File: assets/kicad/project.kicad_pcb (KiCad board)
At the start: 2 copper layers, 150.2 x 91.2 mm, 27 parts, among them J1 Adafruit microSD, J2 EPD, J3 RTC

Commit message: added delay
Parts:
- renumbered R2 to R1, R1 to R2
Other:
- board text added: "21.06.2025"
- board text added: "Alessandro Crugnola"
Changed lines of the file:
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@@
 		(property "Value" "RTC"
 			(at 17.526 6.35 0)
-			(layer "F.Fab")
+			(layer "F.SilkS")
 			(effects
 				(font
@@
 		(descr "Resistor, Axial_DIN0207 series, Axial, Horizontal, pin pitch=7.62mm, 0.25W = 1/4W, length*diameter=6.3*2.5mm^2, http://cdn-reichelt.de/documents/datenblatt/B400/1_4W%23YAG.pdf")
 		(tags "Resistor Axial_DIN0207 series Axial Horizontal pin pitch 7.62mm 0.25W = 1/4W length 6.3mm diameter 2.5mm")
-		(property "Reference" "R2"
+		(property "Reference" "R1"
 			(at 3.81 -2.37 0)
 			(layer "F.SilkS")
@@
 		(descr "Resistor, Axial_DIN0207 series, Axial, Horizontal, pin pitch=7.62mm, 0.25W = 1/4W, length*diameter=6.3*2.5mm^2, http://cdn-reichelt.de/documents/datenblatt/B400/1_4W%23YAG.pdf")
 		(tags "Resistor Axial_DIN0207 series Axial Horizontal pin pitch 7.62mm 0.25W = 1/4W length 6.3mm diameter 2.5mm")
-		(property "Reference" "R1"
+		(property "Reference" "R2"
 			(at 3.81 -2.37 0)
 			(layer "F.SilkS")
@@
 		)
 	)
+	(gr_text "21.06.2025"
+		(at 206.756 193.548 0)
+		(layer "Cmts.User")
+		(effects
+			(font
+				(size 1 1)
+				(thickness 0.1)
+			)
+			(justify left bottom)
+		)
+	)
+	(gr_text "Alessandro Crugnola"
+		(at 178.054 172.212 0)
+		(layer "Cmts.User")
+		(effects
+			(font
+				(size 2 2)
+				(thickness 0.1)
+			)
+			(justify left bottom)
+		)
+	)
+	(gr_text "Photo Frame"
+		(at 186.69 190.5 0)
+		(layer "Cmts.User")
+		(effects
+			(font
+				(size 2 2)
+				(thickness 0.25)
+			)
+			(justify left bottom)
+		)
+	)

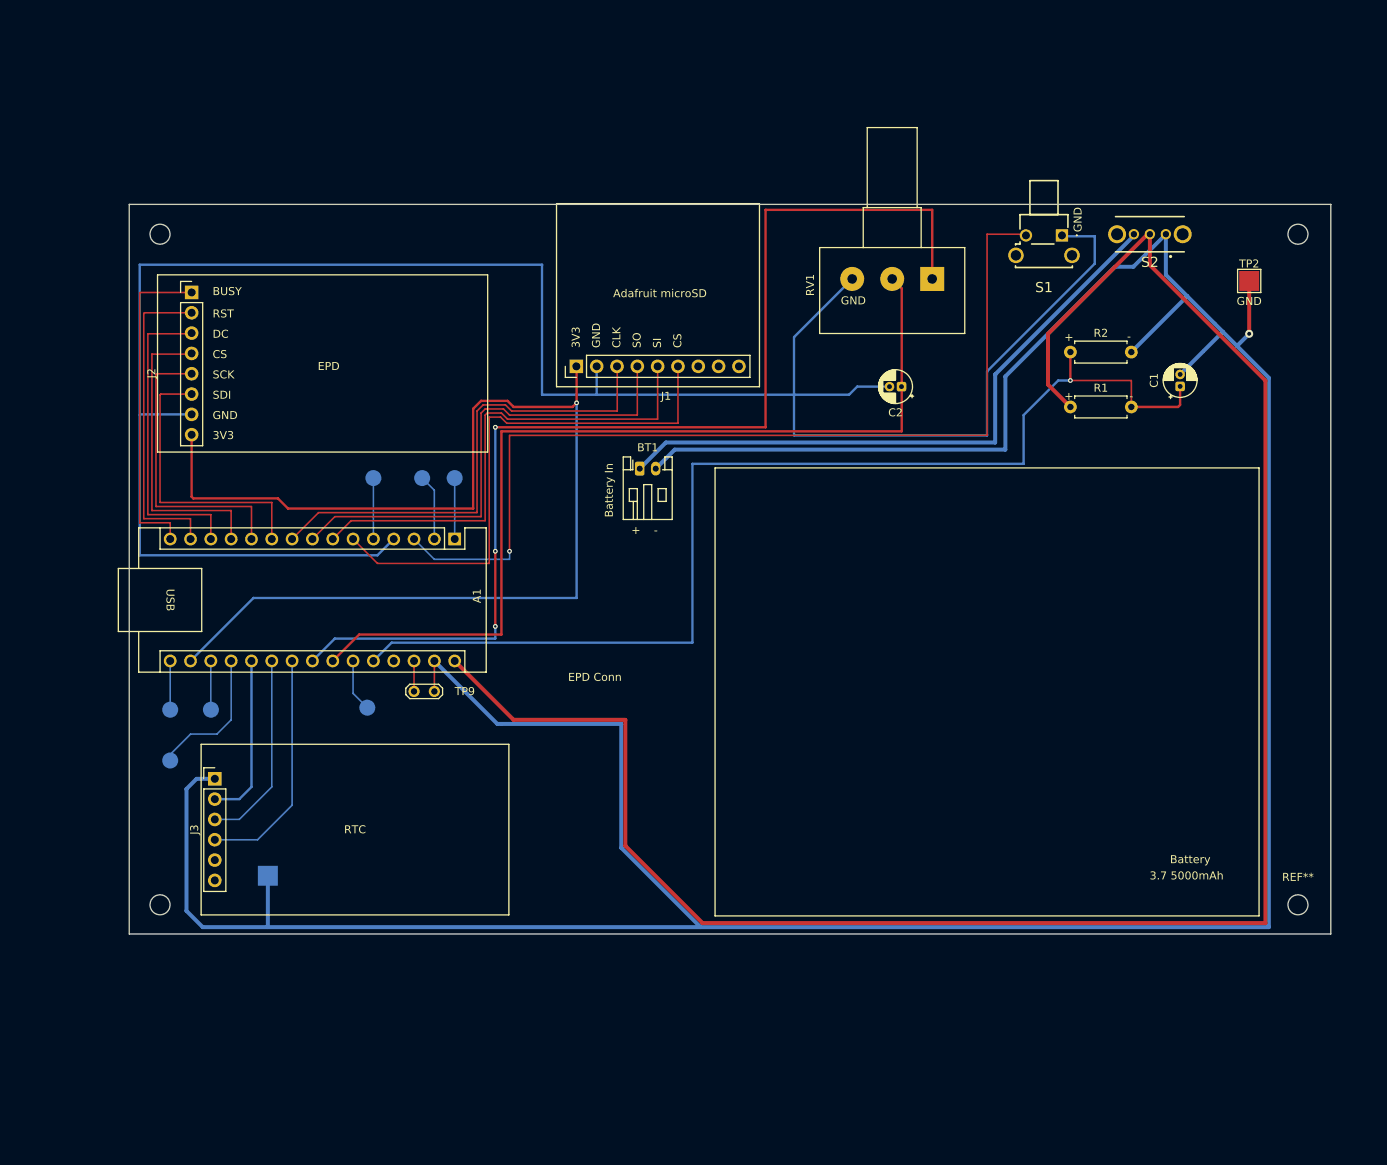
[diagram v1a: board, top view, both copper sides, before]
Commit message: updated pins
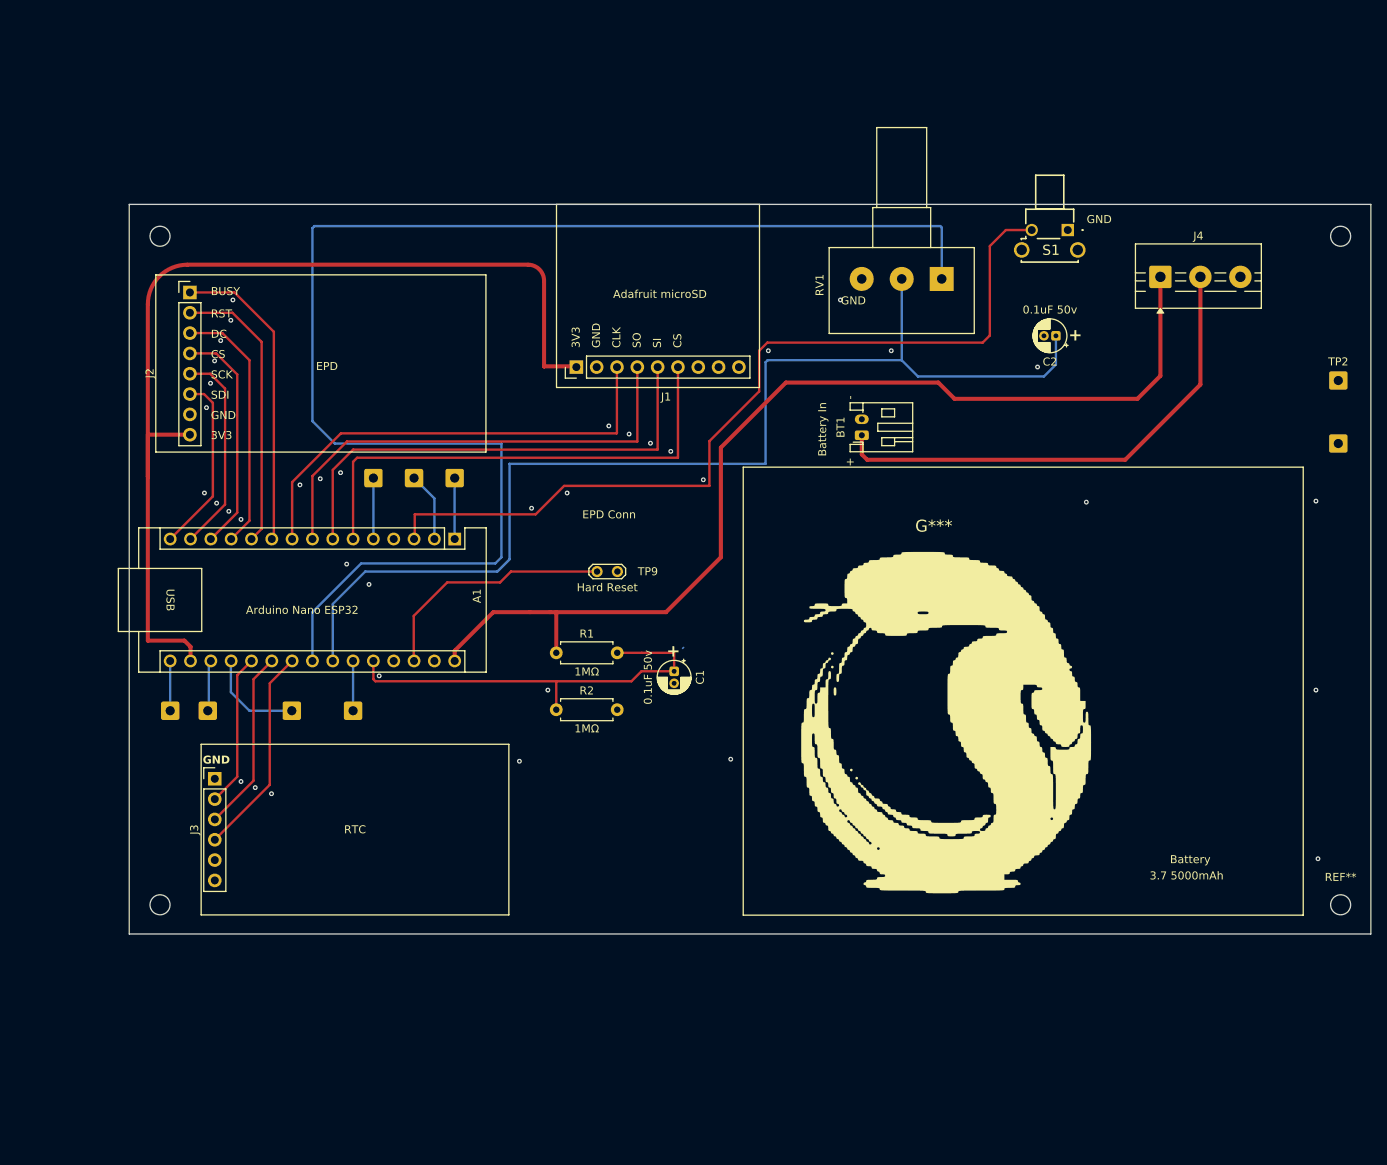
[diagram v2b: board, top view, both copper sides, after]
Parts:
- removed S2: OS102011MA1QN1, Mouser:Switch Button - OS102011MA1QN1
- added G***: LOGO, Sephiroth:Sepy, F.Cu at (173.8, 125.6)
- added J4: Screw_Terminal_01x03, TerminalBlock:TerminalBlock_MaiXu_MX126-5.0-03P_1x03_P5.00mm, F.Cu at (201.8, 69.6)
- TP1, TP2: footprint TestPoint:TestPoint_Pad_2.5x2.5mm -> Connector_Wire:SolderWire-0.5sqmm_1x01_D0.9mm_OD2.3mm
- TP10, TP3, TP4, TP5, TP6, TP7, TP8: footprint TestPoint:TestPoint_Pad_D2.0mm -> Connector_Wire:SolderWire-0.5sqmm_1x01_D0.9mm_OD2.3mm
- moved TP1 144.3 mm to (224.0, 90.4)
- moved R2 78.3 mm to (126.2, 123.7)
- moved C1 72.6 mm to (141.0, 118.9), turned to -90 degrees
- moved R1 71.2 mm to (126.2, 116.6)
- moved BT1 28.1 mm to (164.4, 89.4), turned to 90 degrees
- moved TP9 27.4 mm to (131.3, 106.4)
- moved REF** 20.4 mm to (133.1, 101.6)
- moved C2 20.3 mm to (188.7, 77.0)
- moved TP2 16.7 mm to (224.0, 82.5)
- moved TP3 16.4 mm to (93.2, 123.8)
- moved REF** 5.34 mm to (224.3, 64.5)
- moved REF** 5.33 mm to (224.3, 148.1)
- moved TP8 1.82 mm to (100.8, 123.8)
- moved RV1 1.19 mm to (174.4, 69.8)
- moved TP7 1.02 mm to (108.5, 94.7)
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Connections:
- net Net-(A1-3V3) renamed /3V3
- net Net-(A1-D3) renamed /CS (1)
- net Net-(A1-D4) renamed /DI
- net Net-(A1-D5) renamed /DO
- net Net-(A1-D6) renamed /SCLK
- A1 pad 10: Net-(A1-D7) -> /BUSY
- A1 pad 11: Net-(A1-D8) -> /RST
- A1 pad 12: Net-(A1-D9) -> /DC
- A1 pad 13: Net-(A1-D10/CS) -> /CS
- A1 pad 14: Net-(A1-D11/COPI) -> /SCK
- A1 pad 15: Net-(A1-D12/CIPO) -> /SDI
- BT1 pad 1: Net-(BT1-+) -> /VIN
- J2 pad 1: Net-(A1-D12/CIPO) -> /BUSY
- J2 pad 2: Net-(A1-D11/COPI) -> /RST
- J2 pad 3: Net-(A1-D10/CS) -> /DC
- J2 pad 4: Net-(A1-D9) -> /CS
- J2 pad 5: Net-(A1-D8) -> /SCK
- J2 pad 6: Net-(A1-D7) -> /SDI
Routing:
- net GND: track 692.5 -> 1.06 mm, vias 1 -> 37
- net +4V: track 244.4 -> 130.9 mm
- net Net-(A1-A7): track 141.3 -> 53.5 mm, vias 1 -> 0
- net Net-(BT1-+): track 79.0 -> 0.00 mm
- net /VIN: track 0.00 -> 62.4 mm
- net Net-(A1-D12/CIPO): track 41.1 -> 0.00 mm
- net Net-(A1-SDA/A4): track 140.9 -> 181.0 mm, vias 3 -> 0
- net Net-(A1-D11/COPI): track 40.1 -> 0.00 mm
- net Net-(A1-D10/CS): track 39.0 -> 0.00 mm
- net /BUSY: track 0.00 -> 38.5 mm
- net Net-(A1-D9): track 38.0 -> 0.00 mm
- net Net-(A1-D8): track 37.0 -> 0.00 mm
- net Net-(A1-D7): track 36.0 -> 0.00 mm
- net /RST: track 0.00 -> 35.6 mm
- net /DC: track 0.00 -> 32.1 mm
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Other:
- board size 150.2 x 91.2 mm -> 155.2 x 91.2 mm

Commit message: added support for 6 color e-display
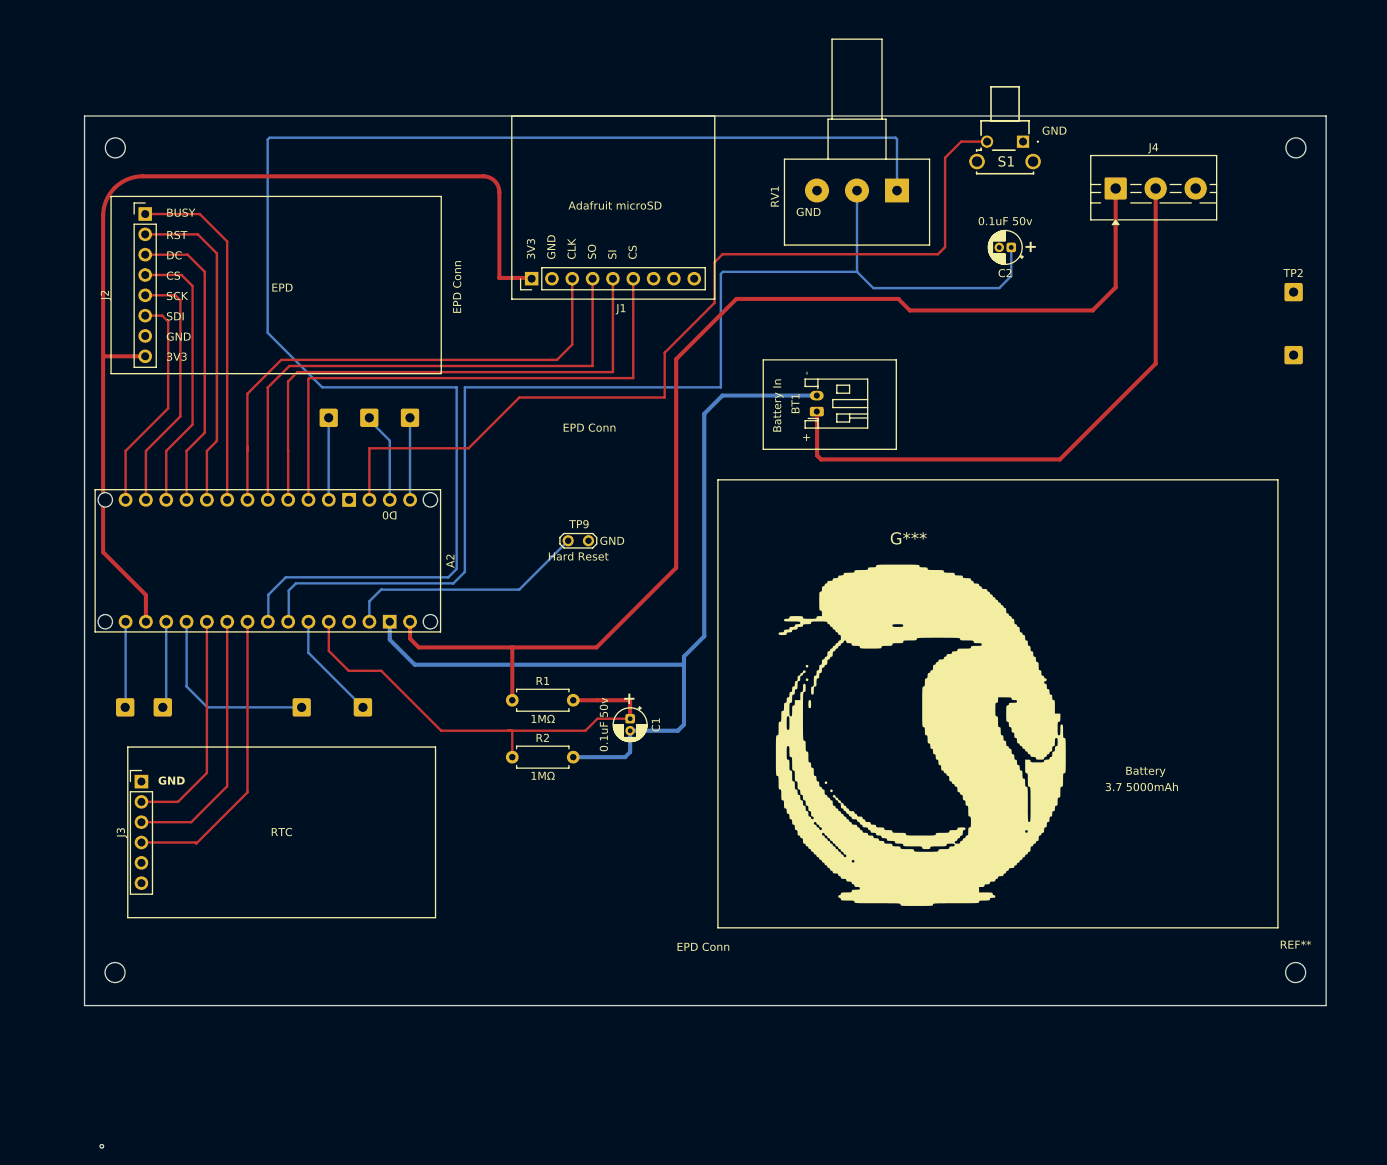
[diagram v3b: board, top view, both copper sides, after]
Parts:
- removed A1: Arduino Nano ESP32, Module:Arduino_Nano
- added A2: Arduino_Nano_ESP32_Socket, PCM_arduino-library:Arduino_Nano_ESP32_Socket, F.Cu at (68.6, 105.1)
- added REF**: EPD Conn, MountingHole:MountingHole 14x1mm_Pad, F.Cu at (144.9, 155.7)
- added REF**: EPD Conn, MountingHole:MountingHole 14x1mm_Pad, F.Cu at (116.2, 70.6)
- TP3: value A0/D17 -> A0
- TP8: value A6/D23 -> A6
- moved J4 12.4 mm to (196.2, 58.5)
- moved REF** 12.4 mm to (218.7, 53.5)
- moved TP1 12.4 mm to (218.4, 79.4)
- moved TP2 12.4 mm to (218.4, 71.5)
- moved C2 12.4 mm to (183.1, 65.9)
- moved J1 12.4 mm to (123.2, 69.8)
- moved REF** 12.4 mm to (71.1, 53.5)
- moved S1 12.4 mm to (184.6, 52.7)
- moved RV1 12.4 mm to (168.8, 58.8)
- moved J2 11.3 mm to (74.9, 61.7)
- moved REF** 11.1 mm to (130.6, 90.8)
- moved REF** 10.2 mm to (71.1, 156.6)
- moved REF** 10.2 mm to (218.7, 156.6)
- moved TP5 9.38 mm to (97.8, 87.2)
- moved TP6 9.38 mm to (107.9, 87.2)
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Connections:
- net /VIN renamed Net-(BT1-+)
- net Net-(A1-A7) renamed /A7
- net Net-(A1-SCL/A5) renamed /A5
- BT1 pad 2: GND -> GND2
- C1 pad 2: GND -> GND2
- C2 pad 2: GND -> GND1
- J1 pad 2: GND -> GND1
- J1 pad 3: /SCLK -> /D6
- J1 pad 4: /DO -> /D5
- J1 pad 5: /DI -> /D4
- J1 pad 6: /CS (1) -> /D3
- J2 pad 1: /BUSY -> /D7
- J2 pad 2: /RST -> /D8
- J2 pad 3: /DC -> /D9
- J2 pad 4: /CS -> /D10
- J2 pad 5: /SCK -> /D11
- J2 pad 6: /SDI -> /D12
- J2 pad 7: GND -> GND1
- J3 pad 1: GND -> GND1
- J3 pad 2: Net-(A1-A1) -> /A1
- J3 pad 3: Net-(A1-A2) -> /A2
- J3 pad 4: Net-(A1-A3) -> /A3
- R2 pad 2: GND -> GND2
- RV1 pad 1: Net-(A1-SDA/A4) -> /A4
- RV1 pad 3: GND -> GND1
- S1 pad 1: GND -> GND1
- S1 pad 2: Net-(A1-~{RESET}) -> /RST
- TP1 pad 1: GND -> GND1
- TP10 pad 1: Net-(A1-B0) -> /B0
- TP2 pad 1: GND -> GND1
- TP3 pad 1: Net-(A1-A0) -> /A0
- TP4 pad 1: Net-(A1-D13/SCK) -> /D13
- TP5 pad 1: Net-(A1-D2) -> /D2
- TP6 pad 1: Net-(A1-D1/TX) -> /D1
- TP7 pad 1: Net-(A1-D0/RX) -> /D0
- TP8 pad 1: Net-(A1-A6) -> /A6
- TP9 pad 1: Net-(A1-B1) -> /B1
- TP9 pad 2: GND -> GND1
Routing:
- net /A4: track 0.00 -> 186.8 mm
- net Net-(A1-SDA/A4): track 181.0 -> 0.00 mm
- net GND2: track 0.00 -> 113.0 mm
- net Net-(A1-~{RESET}): track 107.8 -> 0.00 mm
- net /RST: track 35.6 -> 112.3 mm
- net /D3: track 0.00 -> 68.2 mm
- net /D4: track 0.00 -> 67.6 mm
- net /D5: track 0.00 -> 66.7 mm
- net /D6: track 0.00 -> 65.1 mm
- net /CS (1): track 61.8 -> 0.00 mm
- net /DI: track 60.6 -> 0.00 mm
- net /DO: track 59.6 -> 0.00 mm
- net /SCLK: track 58.5 -> 0.00 mm
- net /D7: track 0.00 -> 44.0 mm
- net /D8: track 0.00 -> 41.3 mm
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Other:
- board size 155.2 x 91.2 mm -> 155.2 x 111.2 mm

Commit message: pcb
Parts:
- removed the REF** at (144.9, 155.7)
- removed the REF** at (130.6, 90.8)
- removed the REF** at (116.2, 70.6)
- TP5: moved to F.Cu
- turned TP5 to 0 degrees
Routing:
- net /3V3: track 126.3 -> 211.1 mm, vias 0 -> 2
- net GND2: track 113.0 -> 110.7 mm
- net /A5: track 147.8 -> 146.3 mm
- net +4V: track 144.9 -> 144.2 mm
- net /RST: track 112.3 -> 111.7 mm
- added copper zone on B.Cu, net (none)
- added copper zone on F.Cu, net (none)
- added copper zone on B.Cu, net GND1
- added copper zone on F.Cu, net GND1
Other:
- outline, holes or cut-outs redrawn
